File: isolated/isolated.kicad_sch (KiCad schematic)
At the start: 59 parts, among them J1 Screw_Terminal_01x02, J2 Screw_Terminal_01x02, Q1 IRF3205, Q2 IRF3205, U1 LTC3723, U2 TCMT1103, U3 LT1431, U4 MCP1792x-5002xCB

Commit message: Minor fixes
Signed-off-by: Patrick Rudolph <rudolphpatrick05@gmail.com>
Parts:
- C10: value C_Polarized -> 100u
- C16, C18: footprint Capacitor_THT:C_Radial_D10.0mm_H12.5mm_P5.00mm -> Capacitor_THT:C_Radial_D16.0mm_H25.0mm_P7.50mm
- C17: value 100u -> 10u
- Q1, Q2: value IRF3205 -> IRLIZ 34N
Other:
- note added: "Current sense=300mV 2.7A max"
- note added: "Isolated tab Add 2x "FK 243 MI 247 O""
- note removed: "Current sense=300mV"
- note removed: "DNP"
- note removed: "FK 243 MI 247 O"
- moved on the sheet: D2, R2

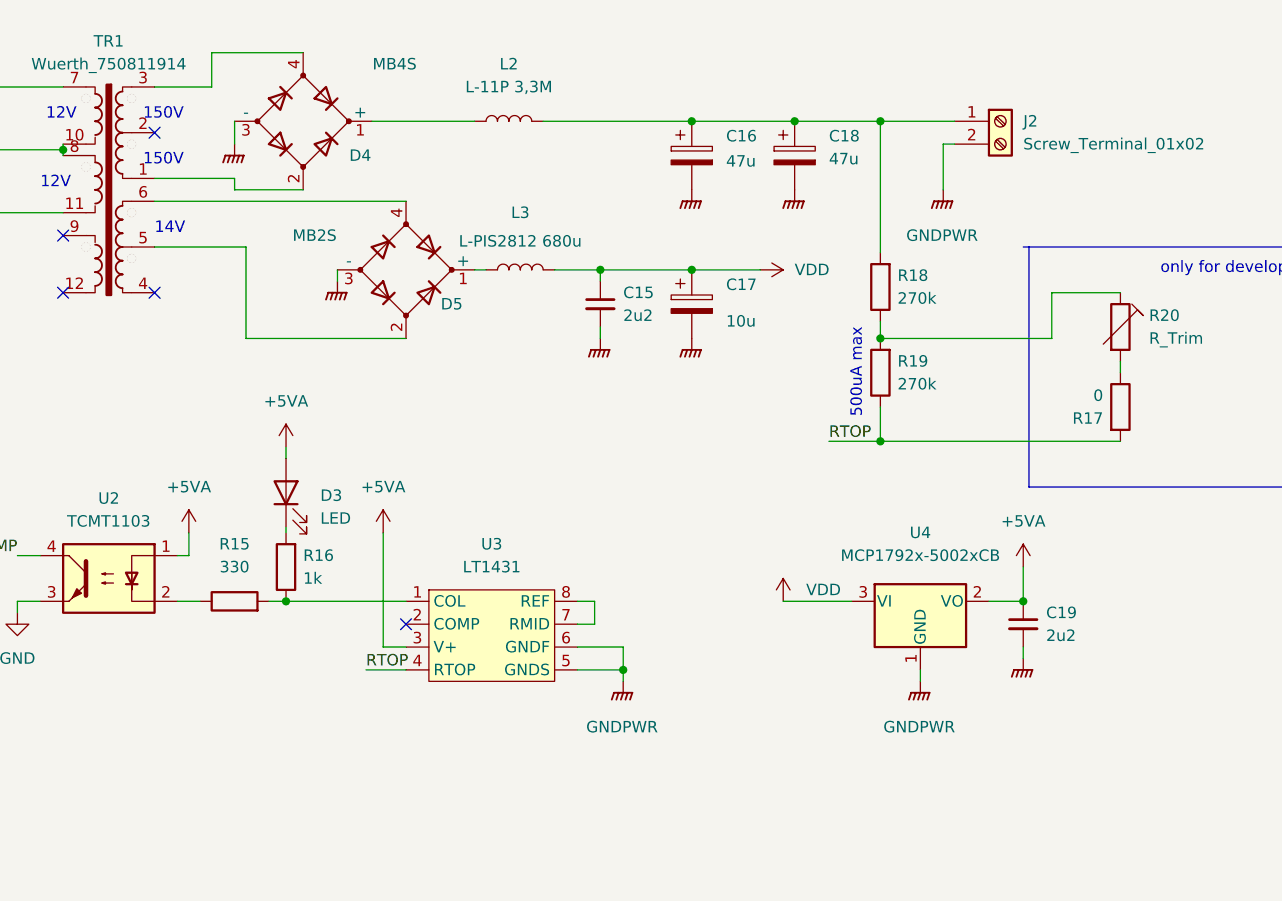
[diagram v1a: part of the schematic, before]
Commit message: kicad: Minor cleanups
- Replace LT1431 with TL431.

Signed-off-by: Patrick Rudolph <rudolphpatrick05@gmail.com>
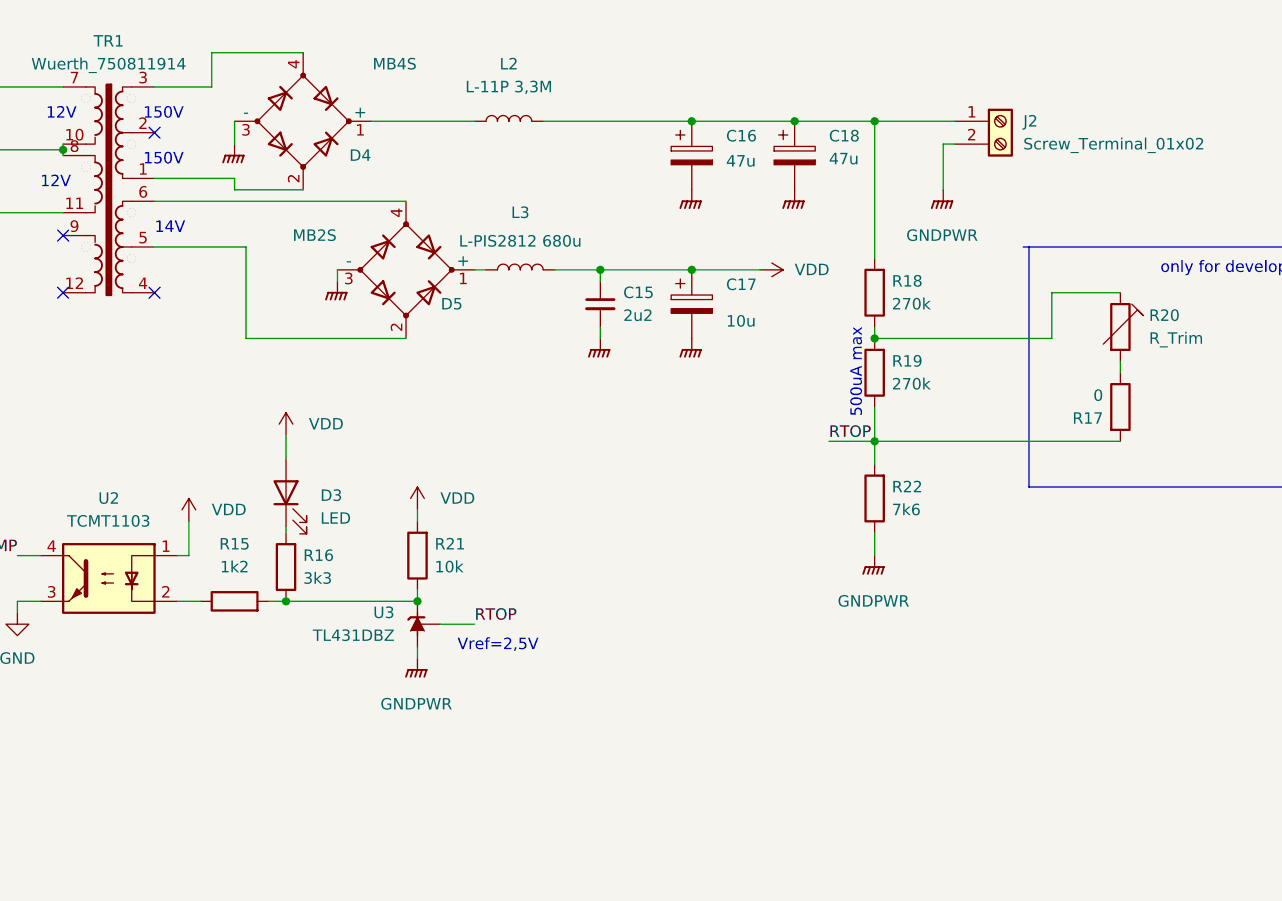
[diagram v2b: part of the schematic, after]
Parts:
- removed C19: 2u2, Capacitor_SMD:C_1210_3225Metric_Pad1.33x2.70mm_HandSolder, symbol Device:C_Small
- removed U3: LT1431, Package_SO:SOIC-8_3.9x4.9mm_P1.27mm, symbol LT1431:LT1431
- removed U4: MCP1792x-5002xCB, Package_TO_SOT_SMD:SOT-23, symbol Regulator_Linear:MCP1792x-5002xCB
- added R21: 10k, Resistor_SMD:R_0805_2012Metric_Pad1.20x1.40mm_HandSolder, symbol Device:R
- added R22: 7k6, Resistor_SMD:R_0805_2012Metric_Pad1.20x1.40mm_HandSolder, symbol Device:R
- added U3: TL431DBZ, Package_TO_SOT_SMD:SOT-23, symbol Reference_Voltage:TL431DBZ
- C16, C18: footprint Capacitor_THT:C_Radial_D16.0mm_H25.0mm_P7.50mm -> Capacitor_THT:C_Radial_D12.5mm_H20.0mm_P5.00mm
- R15: value 330 -> 1k2
- R16: value 1k -> 3k3
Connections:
- net +5VA is gone; now on net VDD: D3.2 (A), U2.1
- net GNDPWR: now also R22.1, U3.3 (A)
- net RTOP: now also R22.2, U3.2 (REF)
- net VDD: now also R21.2
- net at R15.2, R16.1: now also R21.1, U3.1 (K)
- no-connect marks 7 -> 6
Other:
- note added: "Vref=2,5V"
- moved on the sheet: R18, R19

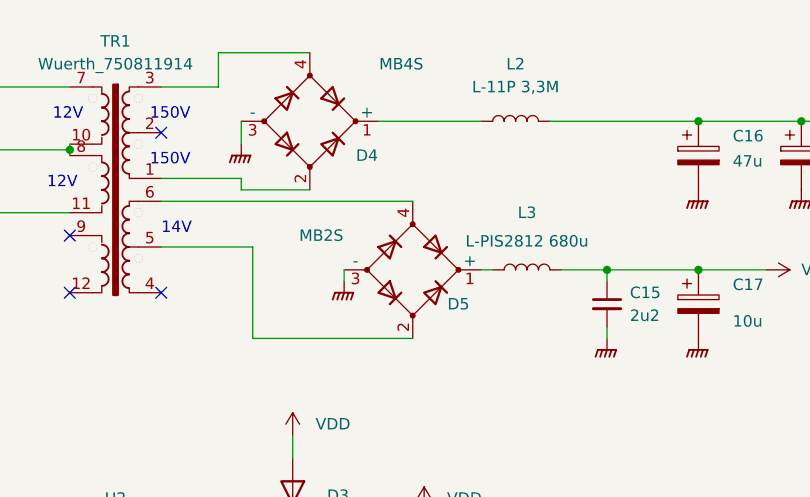
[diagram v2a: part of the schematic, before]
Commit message: kicad: Fix issues found in v0.1
- Change SOIC to SSOP package
- Fix MB4S pinout

Signed-off-by: Patrick Rudolph <rudolphpatrick05@gmail.com>
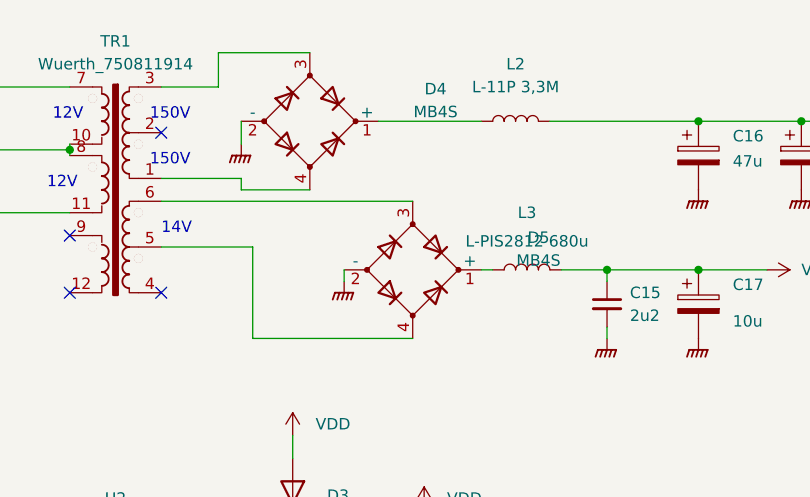
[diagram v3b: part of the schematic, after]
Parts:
- removed D4: MB4S, Package_TO_SOT_SMD:TO-269AA, symbol Device:D_Bridge_+A-A
- removed D5: MB2S, Package_TO_SOT_SMD:TO-269AA, symbol Device:D_Bridge_+A-A
- added D4, D5: MB4S, Package_TO_SOT_SMD:TO-269AA, symbol Device:D_Bridge_+-AA
- U1: footprint Package_SO:SOIC-16_3.9x9.9mm_P1.27mm -> Package_SO:SSOP-16_3.9x4.9mm_P0.635mm
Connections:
- net GNDPWR: now also D4.2 (-), D5.2 (-)
- net at L2.1: now also D4.1 (+)
- net at TR1.1: now also D4.4
- net at TR1.3: now also D4.3
- net at L3.1: now also D5.1 (+)
- net at TR1.5: now also D5.4
- net at TR1.6: now also D5.3
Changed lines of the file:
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@@
     (property "Reference" "U1" (id 0) (at 58.42 101.6 0))
     (property "Value" "LTC3723" (id 1) (at 58.42 104.14 0))
-    (property "Footprint" "Package_SO:SOIC-16_3.9x9.9mm_P1.27mm" (id 2) (at 58.42 128.27 0)
+    (property "Footprint" "Package_SO:SSOP-16_3.9x4.9mm_P0.635mm" (id 2) (at 58.42 128.27 0)
       (effects (font (size 1.27 1.27)) hide)
     )
@@
     (pin "1")
   )
-  (symbol (lib_id "Device:D_Bridge_+A-A") (at 163.83 29.21 0) (unit 1)
-    (in_bom yes) (on_board yes)
-    (property "Reference" "D4" (id 0) (at 170.18 33.02 0))
-    (property "Value" "MB4S" (id 1) (at 173.99 22.86 0))
-    (property "Footprint" "Package_TO_SOT_SMD:TO-269AA" (id 2) (at 163.83 29.21 0)
-      (effects (font (size 1.27 1.27)) hide)
-    )
-    (property "Datasheet" "~" (id 3) (at 163.83 29.21 0)
-      (effects (font (size 1.27 1.27)) hide)
-    )
-    (pin "1")
-    (pin "2")
-    (pin "3")
-    (pin "4")
-  )
   (symbol (lib_id "Device:D_Zener") (at 38.735 73.025 0) (unit 1)
     (in_bom yes) (on_board yes) (fields_autoplaced)
@@
     (pin "1")
   )
-  (symbol (lib_id "Device:D_Bridge_+A-A") (at 175.26 45.72 0) (unit 1)
-    (in_bom yes) (on_board yes)
-    (property "Reference" "D5" (id 0) (at 180.34 49.53 0))
-    (property "Value" "MB2S" (id 1) (at 165.1 41.91 0))
-    (property "Footprint" "Package_TO_SOT_SMD:TO-269AA" (id 2) (at 175.26 45.72 0)
-      (effects (font (size 1.27 1.27)) hide)
-    )
-    (property "Datasheet" "~" (id 3) (at 175.26 45.72 0)
-      (effects (font (size 1.27 1.27)) hide)
-    )
-    (pin "1")
-    (pin "2")
-    (pin "3")
-    (pin "4")
-  )
   (symbol (lib_id "power:VDD") (at 161.925 64.135 0) (unit 1)
     (in_bom yes) (on_board yes) (fields_autoplaced)
@@
     (pin "4")
   )
+  (symbol (lib_id "Device:D_Bridge_+-AA") (at 175.26 45.72 0) (unit 1)
+    (in_bom yes) (on_board yes) (fields_autoplaced)
+    (property "Reference" "D5" (id 0) (at 189.23 42.1386 0))
+    (property "Value" "MB4S" (id 1) (at 189.23 44.6786 0))
+    (property "Footprint" "Package_TO_SOT_SMD:TO-269AA" (id 2) (at 175.26 45.72 0)
+      (effects (font (size 1.27 1.27)) hide)
+    )
+    (property "Datasheet" "~" (id 3) (at 175.26 45.72 0)
+      (effects (font (size 1.27 1.27)) hide)
+    )
+    (pin "1")
+    (pin "2")
+    (pin "3")
+    (pin "4")
+  )
   (symbol (lib_id "Mechanical:MountingHole") (at 167.64 131.445 0) (unit 1)
     (in_bom yes) (on_board yes) (fields_autoplaced)
@@
     (pin "1")
     (pin "2")
+  )
+  (symbol (lib_id "Device:D_Bridge_+-AA") (at 163.83 29.21 0) (unit 1)
+    (in_bom yes) (on_board yes) (fields_autoplaced)
+    (property "Reference" "D4" (id 0) (at 177.8 25.6286 0))
+    (property "Value" "MB4S" (id 1) (at 177.8 28.1686 0))
+    (property "Footprint" "Package_TO_SOT_SMD:TO-269AA" (id 2) (at 163.83 29.21 0)
+      (effects (font (size 1.27 1.27)) hide)
+    )
+    (property "Datasheet" "~" (id 3) (at 163.83 29.21 0)
+      (effects (font (size 1.27 1.27)) hide)
+    )
+    (pin "1")
+    (pin "2")
+    (pin "3")
+    (pin "4")
   )
   (symbol (lib_id "Device:C_Small") (at 196.85 49.53 0) (unit 1)
@@
       (reference "D3") (unit 1) (value "LED") (footprint "LED_THT:LED_D3.0mm_Clear")
     )
-    (path "/1b8d97ef-2f14-4222-b65f-3f6d98e924ba"
+    (path "/b705a48c-035f-4a5b-b97d-b8e8e9a7bb3a"
       (reference "D4") (unit 1) (value "MB4S") (footprint "Package_TO_SOT_SMD:TO-269AA")
     )
-    (path "/6f13df7a-edf7-4ca2-a4eb-31f650574d29"
-      (reference "D5") (unit 1) (value "MB2S") (footprint "Package_TO_SOT_SMD:TO-269AA")
+    (path "/811e164d-beee-455b-92c1-abfc6d476a96"
+      (reference "D5") (unit 1) (value "MB4S") (footprint "Package_TO_SOT_SMD:TO-269AA")
     )
     (path "/df573583-72fa-4edf-a8b4-6bbacfd1d7a5"
@@
     )
     (path "/01bb1f0f-a949-459f-bf40-9ed89259200c"
-      (reference "U1") (unit 1) (value "LTC3723") (footprint "Package_SO:SOIC-16_3.9x9.9mm_P1.27mm")
+      (reference "U1") (unit 1) (value "LTC3723") (footprint "Package_SO:SSOP-16_3.9x4.9mm_P0.635mm")
     )
     (path "/7c3ecda7-235a-424a-af7f-2fd18a2d2abd"
